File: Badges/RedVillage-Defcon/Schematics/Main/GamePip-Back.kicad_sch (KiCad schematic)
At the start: 50 parts, among them J1 2.8" Display, J10 Conn_01x01, J11 Conn_01x01, J12 Conn_01x01, J13 Conn_02x03_Odd_Even, J14 Conn_01x03, J2 USB_C_Plug_USB2.0, J3 Conn_01x03, J4 Cap Sense, J5 Cap Sense, J6 Cap Sense, J8 Conn_01x04, J9 Conn_01x01, Q1 Q_PMOS_DGS, Q2 Q_NPN_BCE, SW1 Up, SW10 Power, SW2 Down, SW3 Left, SW4 A, SW5 Right, SW6 B, SW7 Start/Sel, SW9 RotaryEncoder_Switch, U1 XDS_TX4310B, U2 ESP32-S2-SOLO

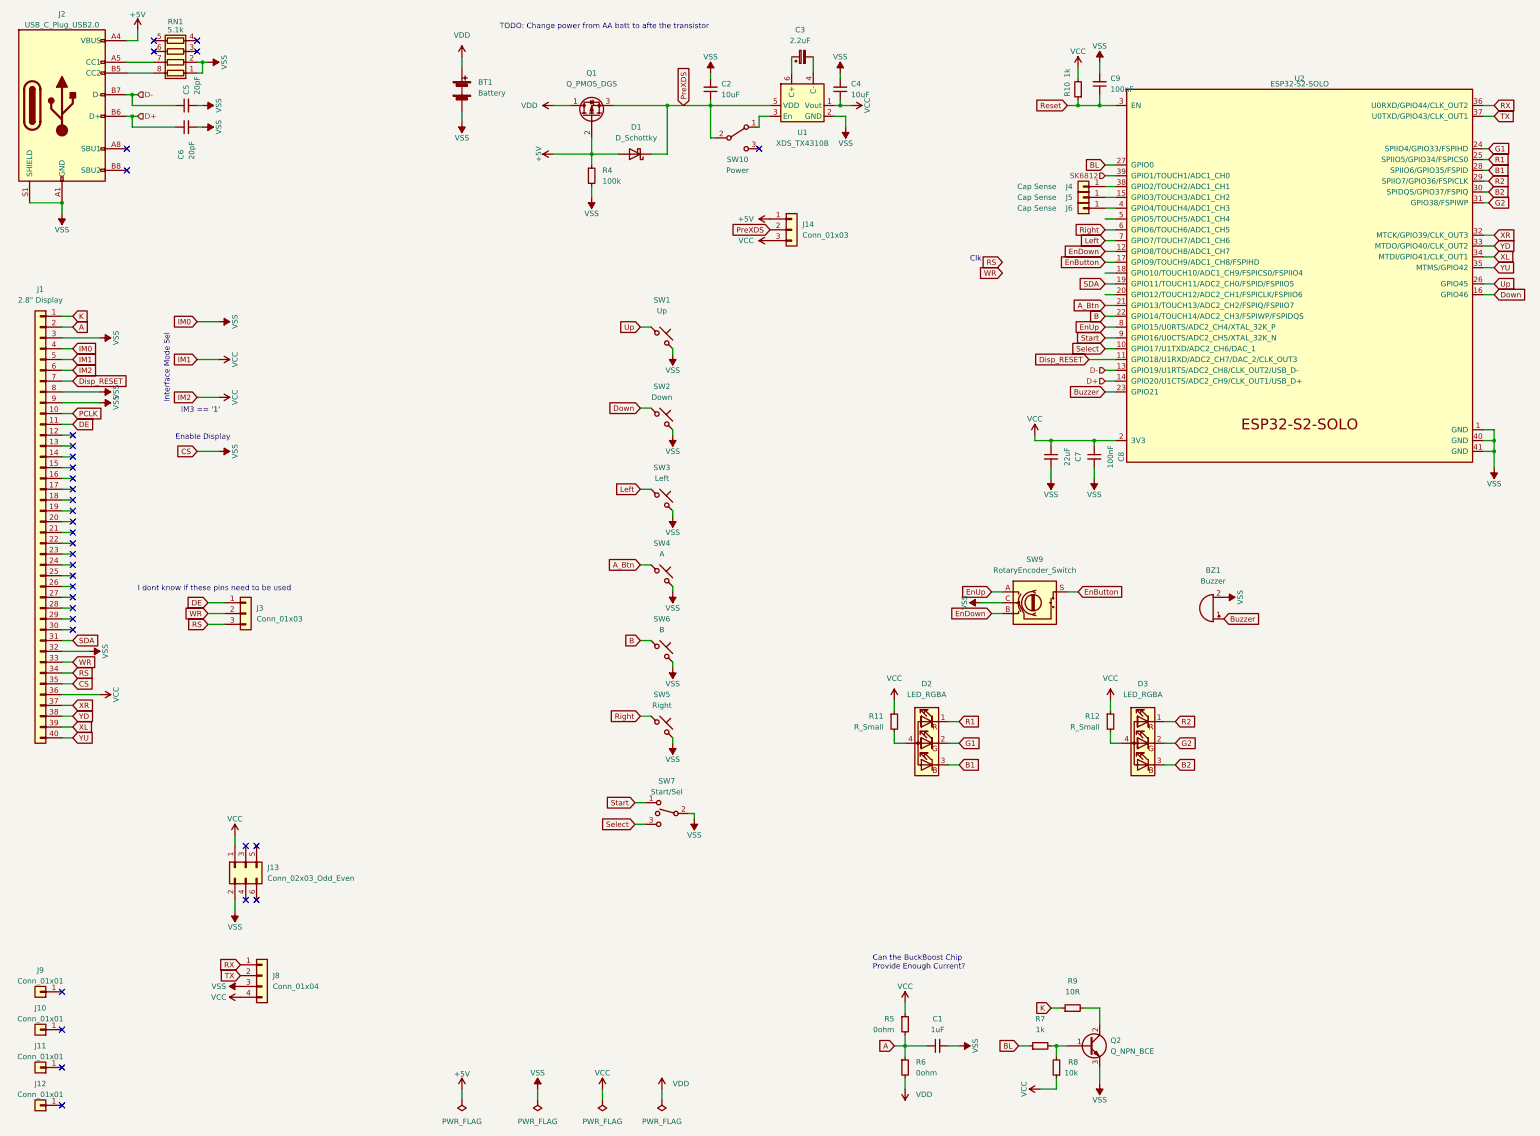
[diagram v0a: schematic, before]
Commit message: V2 complete, Production quantity ordered
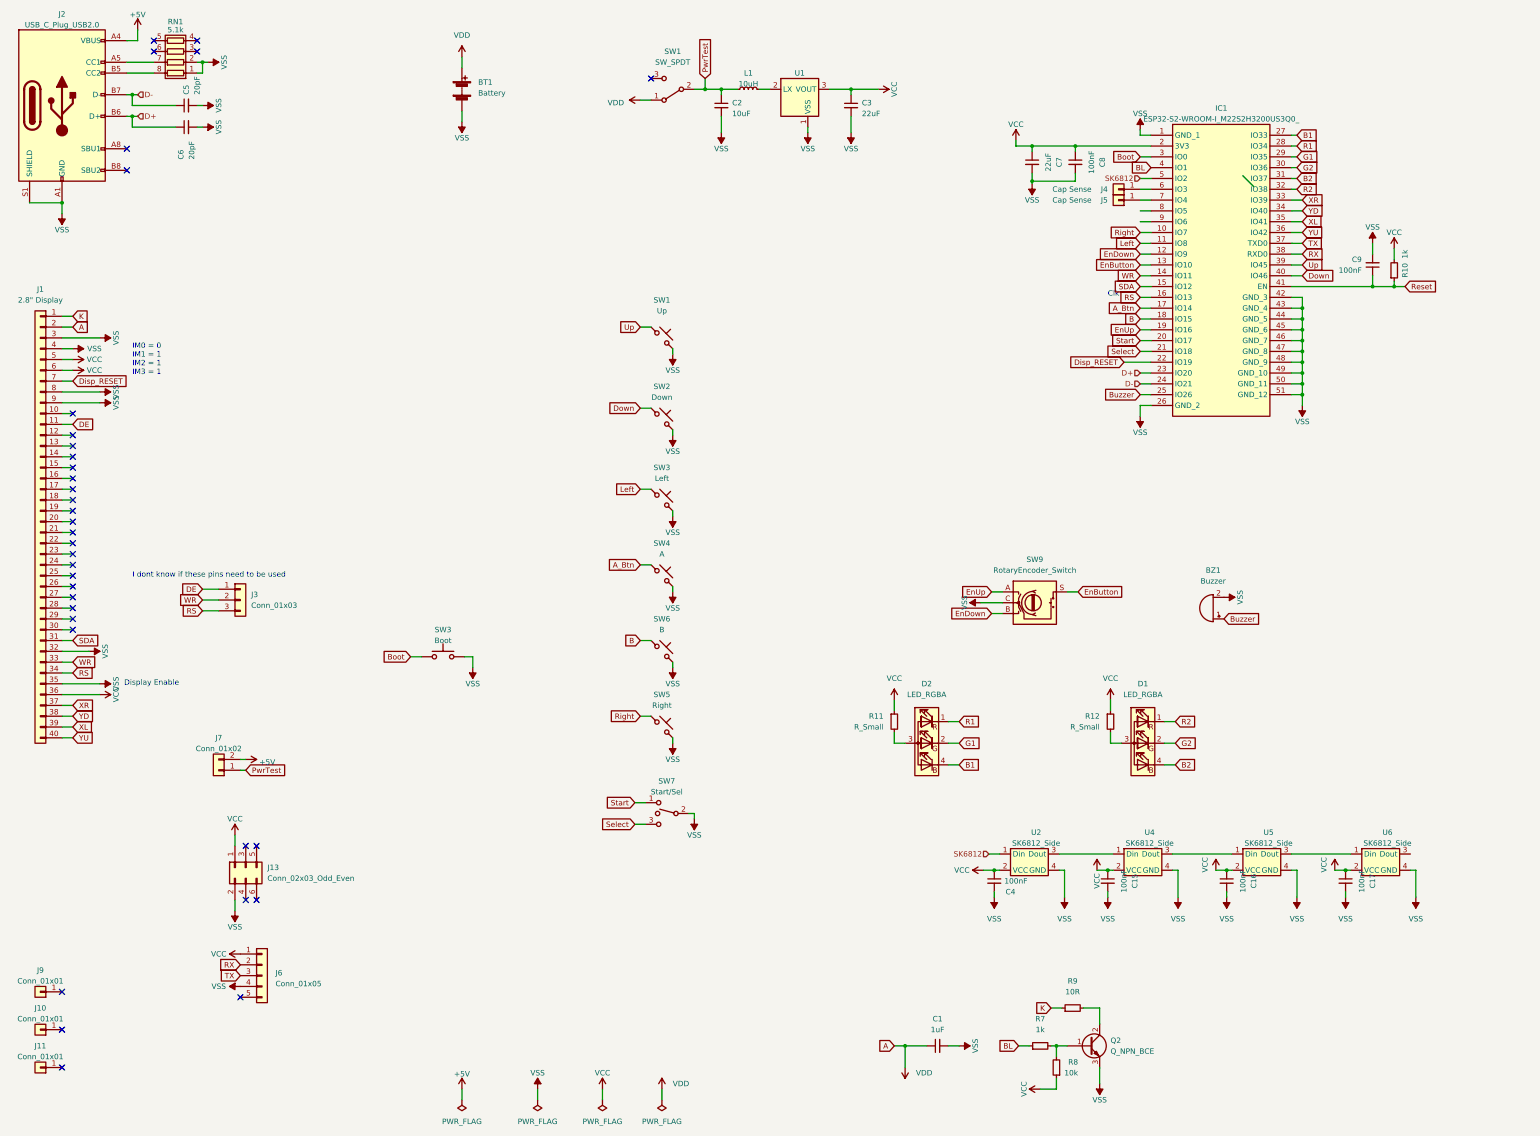
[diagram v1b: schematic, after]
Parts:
- removed C3: 2.2uF, RedVillage:C_0805_2012Metric, symbol Device:C_Polarized_Small
- removed D1: D_Schottky, Diode_SMD:D_SOD-123, symbol Device:D_Schottky
- removed D3: LED_RGBA, RedVillage:XL-3227RGB_LED, symbol Device:LED_RGBA
- removed J12: Conn_01x01, cafebabe:SMD Spacer M2.5, symbol Connector_Generic:Conn_01x01
- removed J14: Conn_01x03, Connector_PinSocket_2.54mm:PinSocket_1x03_P2.54mm_Vertical, symbol Connector_Generic:Conn_01x03
- removed J6: Cap Sense, Bsides22:CapSense, symbol Connector_Generic:Conn_01x01
- removed J8: Conn_01x04, Connector_PinSocket_2.54mm:PinSocket_1x04_P2.54mm_Vertical, symbol Connector_Generic:Conn_01x04
- removed Q1: Q_PMOS_DGS, Package_TO_SOT_SMD:SOT-23, symbol Device:Q_PMOS_DGS
- removed R4: 100k, Resistor_SMD:R_0805_2012Metric, symbol Device:R_Small
- removed R5, R6: 0ohm, Resistor_SMD:R_0805_2012Metric, symbol Device:R_Small
- removed SW10: Power, UE-ButtonSwitch:SK-3296S_switch, symbol Switch:SW_SPDT
- removed U1: XDS_TX4310B, Package_TO_SOT_SMD:TSOT-23-6_HandSoldering, symbol ESP32_C3:XDS_TX4310B
- removed U2: ESP32-S2-SOLO, Espressif:ESP32-S2-SOLO, symbol Espressif:ESP32-S2-SOLO
- added C15, C16, C17: 100nF, Capacitor_SMD:C_0805_2012Metric, symbol Device:C_Small
- added C3: 22uF, Capacitor_SMD:C_0805_2012Metric, symbol Device:C_Small
- added D1: LED_RGBA, RedVillage:XL-3227RGB_LED, symbol Device:LED_RGBA
- added IC1: ESP32-S2-WROOM-I_M22S2H3200US3Q0_, KiCad:ESP32S2WROOMIM22S2H3200US3Q0, symbol ESP32-S2-WROOM-I_M22S2H3200US3:ESP32-S2-WROOM-I_M22S2H3200US3Q0_
- added J6: Conn_01x05, Connector_PinHeader_2.54mm:PinHeader_1x05_P2.54mm_Vertical, symbol Connector_Generic:Conn_01x05
- added J7: Conn_01x02, Connector_PinHeader_2.54mm:PinHeader_1x02_P2.54mm_Vertical, symbol Connector_Generic:Conn_01x02
- added L1: 10uH, Inductor_SMD:L_0805_2012Metric, symbol Device:L_Small
- added SW1: SW_SPDT, BreadBoardPwr:SK-3296S_switch, symbol Switch:SW_SPDT
- added SW3: Boot, Button_Switch_SMD:SW_SPST_SKQG_WithoutStem, symbol Switch:SW_Push
- added U1: ~, Package_TO_SOT_SMD:SOT-23, symbol UE-Power:XT1861B332MR-G
- added U2, U4, U5, U6: SK6812_Side, Bsides22:SK6812_Side, symbol BSides22:SK6812_Side
- C4: value 10uF -> 100nF
- J10, J11, J9: footprint cafebabe:SMD Spacer M2.5 -> RedVillage:Threaded_Standoffs
- J4: footprint CornConStranger:CapSence -> Bsides22:CapSense
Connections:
- net A is gone; now on net VDD: C1.1, J1.2 (Pin_2)
- net +5V: now also J7.2 (Pin_2)
- net A_Btn: now also IC1.17 (IO14)
- net B: now also IC1.18 (IO15)
- net B1: now also D2.4 (BK), IC1.27 (IO33); no longer D2.3 (BK)
- net B2: now also D1.4 (BK), IC1.31 (IO37)
- net BL: now also IC1.4 (IO1)
- net Buzzer: now also IC1.25 (IO26)
- net D+: now also IC1.23 (IO20)
- net D-: now also IC1.24 (IO21)
- net Disp_RESET: now also IC1.22 (IO19)
- net Down: now also IC1.40 (IO46)
- net EnButton: now also IC1.13 (IO10)
- net EnDown: now also IC1.12 (IO9)
- net EnUp: now also IC1.19 (IO16)
- net G1: now also IC1.29 (IO35)
- net G2: now also D1.2 (GK), IC1.30 (IO36)
- net Left: now also IC1.11 (IO8)
- net R1: now also IC1.28 (IO34)
- net R2: now also D1.1 (RK), IC1.32 (IO38)
- net RS: now also IC1.16 (IO13)
- net RX: now also IC1.38 (RXD0), J6.2 (Pin_2)
- net Reset: now also IC1.41 (EN)
- net Right: now also IC1.10 (IO7)
- net SDA: now also IC1.15 (IO12)
- net SK6812: now also IC1.5 (IO2), U2.1 (Din)
- net Select: now also IC1.21 (IO18)
- net Start: now also IC1.20 (IO17)
- net TX: now also IC1.37 (TXD0), J6.3 (Pin_3)
- net Up: now also IC1.39 (IO45)
- net VCC: now also C15.1, C16.1, C17.1, C3.1, IC1.2 (3V3), J6.1 (Pin_1), U1.3 (VOUT), U2.2 (VCC), U4.2 (VCC), U5.2 (VCC), U6.2 (VCC)
- net VDD: now also SW1.1 (A)
- net VSS: now also C15.2, C16.2, C17.2, C3.2, IC1.1 (GND_1), IC1.26 (GND_2), IC1.42 (GND_3), IC1.43 (GND_4), IC1.44 (GND_5), IC1.45 (GND_6), IC1.46 (GND_7), IC1.47 (GND_8), IC1.48 (GND_9), IC1.49 (GND_10), IC1.50 (GND_11), IC1.51 (GND_12), J6.4 (Pin_4), SW3.2, U1.1 (VSS), U2.4 (GND), U4.4 (GND), U5.4 (GND), U6.4 (GND)
- net WR: now also IC1.14 (IO11)
- net XL: now also IC1.35 (IO41)
- net XR: now also IC1.33 (IO39)
- net YD: now also IC1.34 (IO40)
- net YU: now also IC1.36 (IO42)
- net at R12.2: now also D1.3 (A)
- net at J5.1 (Pin_1): now also IC1.7 (IO4)
- net at J4.1 (Pin_1): now also IC1.6 (IO3)
- net at R11.2: now also D2.3 (A); no longer D2.4 (A)
- net PCLK: no longer names the net of J1.10 (Pin_10)
- net PreXDS renamed PwrTest
- net PwrTest: now also J7.1 (Pin_1), L1.1, SW1.2 (B)
- new net: U2.3 (Dout), U4.1 (Din)
- new net: U4.3 (Dout), U5.1 (Din)
- new net: U5.3 (Dout), U6.1 (Din)
- new net: L1.2, U1.2 (LX)
- new net Boot: IC1.3 (IO0), SW3.1
- no-connect marks 34 -> 35
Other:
- note added: "Display Enable"
- note added: "IM0 = 0 IM1 = 1 IM2 = 1 IM3 = 1"
- note removed: "Can the BuckBoost Chip Provide Enough Current?"
- note removed: "Enable Display"
- note removed: "IM3 == '1'"
- note removed: "Interface Mode Sel"
- note removed: "TODO: Change power from AA batt to afte the transistor"
- moved on the sheet: C7, C8, C9, J3, J4, J5, R10

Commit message: spring cleaning
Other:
- note added: "DC"
- note added: "MOSI"
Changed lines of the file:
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@@
   (no_connect (at 31.75 143.51))
   (no_connect (at 31.75 128.27))
-  (bus_entry (at 306.705 57.15) (size 2.54 2.54)
-    (stroke (width 0) (type default))
-  )
   (wire (pts (xy 278.765 100.965) (xy 285.115 100.965))
     (stroke (width 0) (type default))
@@
     (effects (font (size 1.27 1.27)) (justify left bottom))
   )
+  (text "MOSI" (at 271.78 83.82 0)
+    (effects (font (size 1.27 1.27)) (justify left bottom))
+  )
+  (text "DC" (at 274.32 81.28 0)
+    (effects (font (size 1.27 1.27)) (justify left bottom))
+  )
